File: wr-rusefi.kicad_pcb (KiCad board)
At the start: 2 copper layers, 94 x 94 mm, 147 parts, among them P101 USB_OTG, P102 CONN_01X08, P103 CONN_01X08, P104 CONN_01X04, P105 CONN_01X08, P106 CONN_01X08, P107 CONN_01X02, P108 USB_OTG, P109 CONN_01X02, P110 CONN_01X06, Q401 IRF540N, Q402 IRF540N, Q403 IRF540N, Q404 IRF540N, Q405 IRF540N, Q406 IRF540N, U101 ISL89410, U102 ISL89410, U103 FT230XS, U104 MAX9924, U105 MCP2562-E/SN, U106 LD1117S33TR, U107 MAX9924, U108 ISL89410, U109 STM32F407VGTx, U110 ISL89410, U201 LM324, U301 LM324, U501 LM7805CT, Y101 Crystal

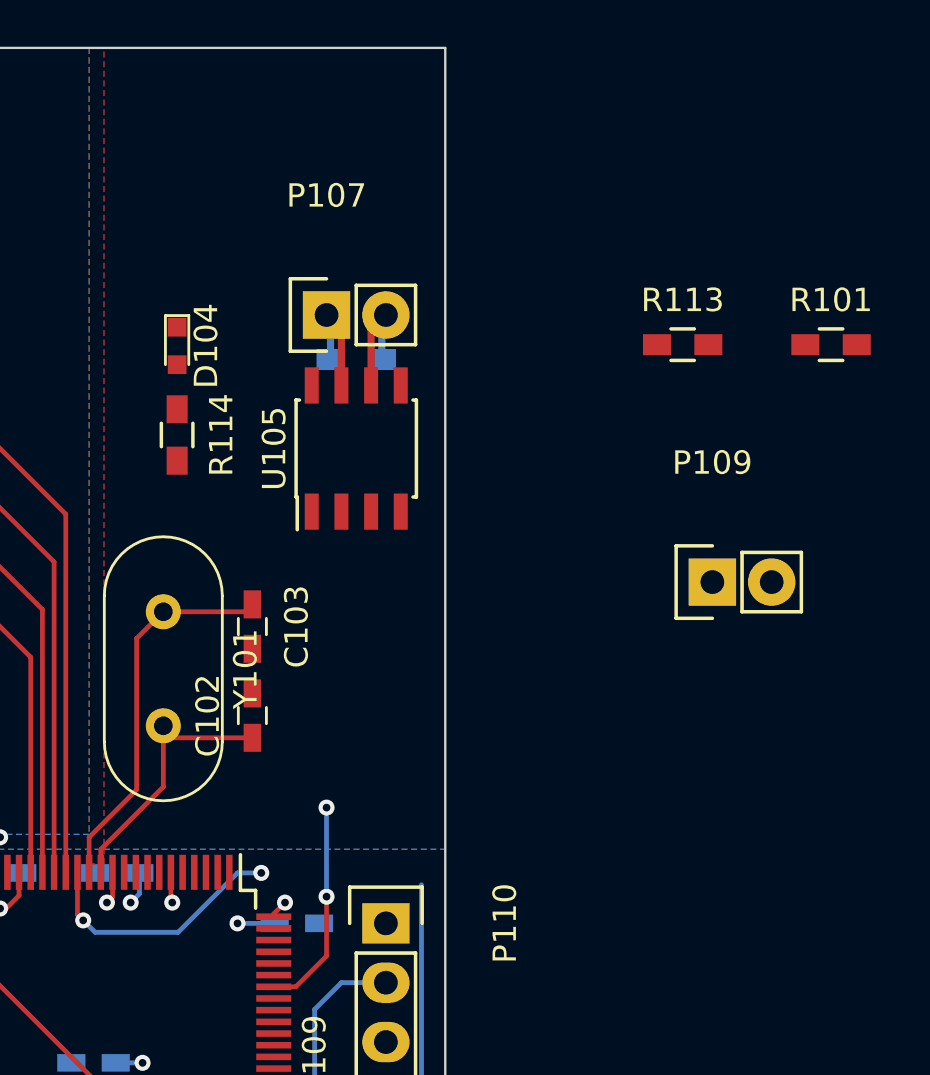
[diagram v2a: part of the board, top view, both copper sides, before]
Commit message: Rough placement of reset & boot0 pullups and jumper
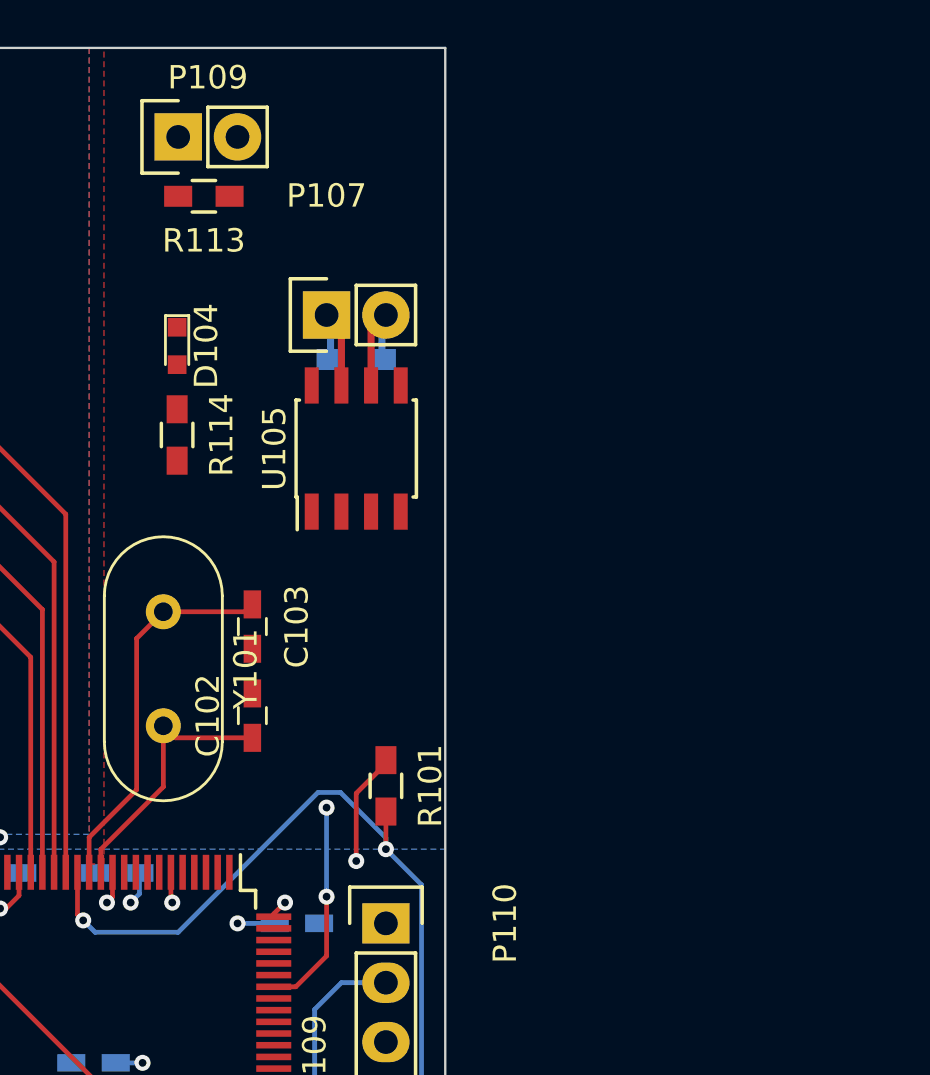
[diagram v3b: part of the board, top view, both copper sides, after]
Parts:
- moved P109 29.8 mm to (133.3, 54.6)
- moved R101 26.8 mm to (142.2, 82.4), turned to 270 degrees
- moved R113 21.5 mm to (134.4, 57.1), turned to 180 degrees
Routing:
- net NRST: track 23.5 -> 35.3 mm
- net +3V3: track 13.7 -> 18.6 mm, vias 8 -> 9
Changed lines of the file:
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@@
     (links 363)
     (no_connects 159)
-    (area 47.1802 29.151866 205.6698 144.830001)
+    (area 47.1802 49.471866 163.619801 144.830001)
     (thickness 1.6)
     (drawings 4)
-    (tracks 929)
+    (tracks 937)
     (zones 0)
     (modules 147)
@@
   )
   (module Socket_Strips:Socket_Strip_Straight_1x02 (layer F.Cu)
-    (at 156.21 73.66)
+    (at 133.35 54.61)
     (descr "Through hole socket strip")
     (tags "socket strip")
-    (fp_text reference P109 (at 0 -5.1) (layer F.SilkS)
+    (fp_text reference P109 (at 1.27 -2.54) (layer F.SilkS)
       (effects (font (size 1 1) (thickness 0.15)))
     )
@@
   )
   (module Resistors_SMD:R_0603_HandSoldering (layer F.Cu)
-    (at 161.29 63.5)
+    (at 142.24 82.38 270)
     (descr "Resistor SMD 0603, hand soldering")
     (tags "resistor 0603")
     (attr smd)
-    (fp_text reference R101 (at 0 -1.9) (layer F.SilkS)
+    (fp_text reference R101 (at 0 -1.9 270) (layer F.SilkS)
       (effects (font (size 1 1) (thickness 0.15)))
     )
-    (fp_text value 10k (at 0 1.9) (layer F.Fab)
+    (fp_text value 10k (at 0 1.9 270) (layer F.Fab)
       (effects (font (size 1 1) (thickness 0.15)))
     )
@@
     (fp_line (start 0.5 0.675) (end -0.5 0.675) (layer F.SilkS) (width 0.15))
     (fp_line (start -0.5 -0.675) (end 0.5 -0.675) (layer F.SilkS) (width 0.15))
-    (pad 1 smd rect (at -1.1 0) (size 1.2 0.9) (layers F.Cu F.Paste F.Mask)
+    (pad 1 smd rect (at -1.1 0 270) (size 1.2 0.9) (layers F.Cu F.Paste F.Mask)
       (net 7 +3V3))
-    (pad 2 smd rect (at 1.1 0) (size 1.2 0.9) (layers F.Cu F.Paste F.Mask)
+    (pad 2 smd rect (at 1.1 0 270) (size 1.2 0.9) (layers F.Cu F.Paste F.Mask)
       (net 94 NRST))
     (model Resistors_SMD.3dshapes/R_0603_HandSoldering.wrl
@@
   )
   (module Resistors_SMD:R_0603_HandSoldering (layer F.Cu)
-    (at 154.94 63.5)
+    (at 134.45 57.15 180)
     (descr "Resistor SMD 0603, hand soldering")
     (tags "resistor 0603")
     (attr smd)
-    (fp_text reference R113 (at 0 -1.9) (layer F.SilkS)
+    (fp_text reference R113 (at 0 -1.9 180) (layer F.SilkS)
       (effects (font (size 1 1) (thickness 0.15)))
     )
-    (fp_text value 10k (at 0 1.9) (layer F.Fab)
+    (fp_text value 10k (at 0 1.9 180) (layer F.Fab)
       (effects (font (size 1 1) (thickness 0.15)))
     )
@@
     (fp_line (start 0.5 0.675) (end -0.5 0.675) (layer F.SilkS) (width 0.15))
     (fp_line (start -0.5 -0.675) (end 0.5 -0.675) (layer F.SilkS) (width 0.15))
-    (pad 1 smd rect (at -1.1 0) (size 1.2 0.9) (layers F.Cu F.Paste F.Mask)
+    (pad 1 smd rect (at -1.1 0 180) (size 1.2 0.9) (layers F.Cu F.Paste F.Mask)
       (net 7 +3V3))
-    (pad 2 smd rect (at 1.1 0) (size 1.2 0.9) (layers F.Cu F.Paste F.Mask)
+    (pad 2 smd rect (at 1.1 0 180) (size 1.2 0.9) (layers F.Cu F.Paste F.Mask)
       (net 91 "Net-(P109-Pad1)"))
     (model Resistors_SMD.3dshapes/R_0603_HandSoldering.wrl
@@
   (segment (start 97.63 58.42) (end 96.52 58.42) (width 0.3048) (layer F.Cu) (net 6))
   (via (at 96.52 58.42) (size 0.6858) (drill 0.3302) (layers F.Cu B.Cu) (net 6))
+  (segment (start 142.24 81.28) (end 142.24 81.43) (width 0.2032) (layer F.Cu) (net 7))
+  (segment (start 142.24 81.43) (end 140.97 82.7) (width 0.2032) (layer F.Cu) (net 7))
+  (segment (start 140.97 82.7) (end 140.97 85.598) (width 0.2032) (layer F.Cu) (net 7))
+  (via (at 140.97 85.598) (size 0.6858) (drill 0.3302) (layers F.Cu B.Cu) (net 7))
   (segment (start 133.04 86.08) (end 133.04 87.32) (width 0.2032) (layer F.Cu) (net 7))
   (segment (start 133.04 87.32) (end 133.096 87.376) (width 0.2032) (layer F.Cu) (net 7))
@@
   (segment (start 136.144 104.394) (end 140.462 100.076) (width 0.2032) (layer B.Cu) (net 93))
   (segment (start 134.874 104.394) (end 136.144 104.394) (width 0.2032) (layer B.Cu) (net 93))
+  (segment (start 129.286 88.138) (end 129.794 88.646) (width 0.2032) (layer B.Cu) (net 94))
+  (segment (start 133.35 88.646) (end 139.331701 82.664299) (width 0.2032) (layer B.Cu) (net 94))
+  (segment (start 129.794 88.646) (end 133.35 88.646) (width 0.2032) (layer B.Cu) (net 94))
+  (segment (start 139.331701 82.664299) (end 140.299232 82.664299) (width 0.2032) (layer B.Cu) (net 94))
+  (segment (start 140.299232 82.664299) (end 142.24 84.605067) (width 0.2032) (layer B.Cu) (net 94))
+  (segment (start 142.24 84.605067) (end 142.24 85.09) (width 0.2032) (layer B.Cu) (net 94))
+  (segment (start 142.24 85.09) (end 142.24 83.48) (width 0.2032) (layer F.Cu) (net 94))
+  (segment (start 143.764 86.614) (end 142.24 85.09) (width 0.2032) (layer B.Cu) (net 94))
+  (via (at 142.24 85.09) (size 0.6858) (drill 0.3302) (layers F.Cu B.Cu) (net 94))
   (segment (start 143.764 96.901) (end 143.764 86.614) (width 0.2032) (layer B.Cu) (net 94))
   (segment (start 142.24 98.425) (end 143.764 96.901) (width 0.2032) (layer B.Cu) (net 94))
-  (segment (start 133.35 88.646) (end 135.89 86.106) (width 0.2032) (layer B.Cu) (net 94))
-  (segment (start 135.89 86.106) (end 136.906 86.106) (width 0.2032) (layer B.Cu) (net 94))
-  (via (at 136.906 86.106) (size 0.6858) (drill 0.3302) (layers F.Cu B.Cu) (net 94))
-  (segment (start 129.794 88.646) (end 133.35 88.646) (width 0.2032) (layer B.Cu) (net 94))
-  (segment (start 129.286 88.138) (end 129.794 88.646) (width 0.2032) (layer B.Cu) (net 94))
   (segment (start 129.04 86.08) (end 129.04 87.892) (width 0.2032) (layer F.Cu) (net 94))
   (segment (start 129.04 87.892) (end 129.286 88.138) (width 0.2032) (layer F.Cu) (net 94))
@@
     (connect_pads (clearance 0.2032))
     (min_thickness 0.2032)
-    (fill (arc_segments 16) (thermal_gap 0.2032) (thermal_bridge_width 0.508))
+    (fill yes (arc_segments 16) (thermal_gap 0.2032) (thermal_bridge_width 0.508))
     (polygon
       (pts
@@
     (connect_pads (clearance 0.2032))
     (min_thickness 0.2032)
-    (fill (arc_segments 16) (thermal_gap 0.2032) (thermal_bridge_width 0.2286))
+    (fill yes (arc_segments 16) (thermal_gap 0.2032) (thermal_bridge_width 0.2286))
     (polygon
       (pts
@@
     (connect_pads (clearance 0.2032))
     (min_thickness 0.2032)
-    (fill (arc_segments 16) (thermal_gap 0.2032) (thermal_bridge_width 0.2286))
+    (fill yes (arc_segments 16) (thermal_gap 0.2032) (thermal_bridge_width 0.2286))
     (polygon
       (pts
@@
     (connect_pads (clearance 0.0254))
     (min_thickness 0.0254)
-    (fill (arc_segments 16) (thermal_gap 0.254) (thermal_bridge_width 0.762))
+    (fill yes (arc_segments 16) (thermal_gap 0.254) (thermal_bridge_width 0.762))
     (polygon
       (pts
@@
     (connect_pads (clearance 0.0254))
     (min_thickness 0.0254)
-    (fill (arc_segments 16) (thermal_gap 0.254) (thermal_bridge_width 0.762))
+    (fill yes (arc_segments 16) (thermal_gap 0.254) (thermal_bridge_width 0.762))
     (polygon
       (pts
@@
     (connect_pads (clearance 0.0254))
     (min_thickness 0.0254)
-    (fill (arc_segments 16) (thermal_gap 0.254) (thermal_bridge_width 0.762))
+    (fill yes (arc_segments 16) (thermal_gap 0.254) (thermal_bridge_width 0.762))
     (polygon
       (pts
@@
     (connect_pads (clearance 0.2032))
     (min_thickness 0.2032)
-    (fill (arc_segments 16) (thermal_gap 0.2032) (thermal_bridge_width 0.508))
+    (fill yes (arc_segments 16) (thermal_gap 0.2032) (thermal_bridge_width 0.508))
     (polygon
       (pts
@@
     (connect_pads (clearance 0.2032))
     (min_thickness 0.2032)
-    (fill (arc_segments 16) (thermal_gap 0.2032) (thermal_bridge_width 0.508))
+    (fill yes (arc_segments 16) (thermal_gap 0.2032) (thermal_bridge_width 0.508))
     (polygon
       (pts

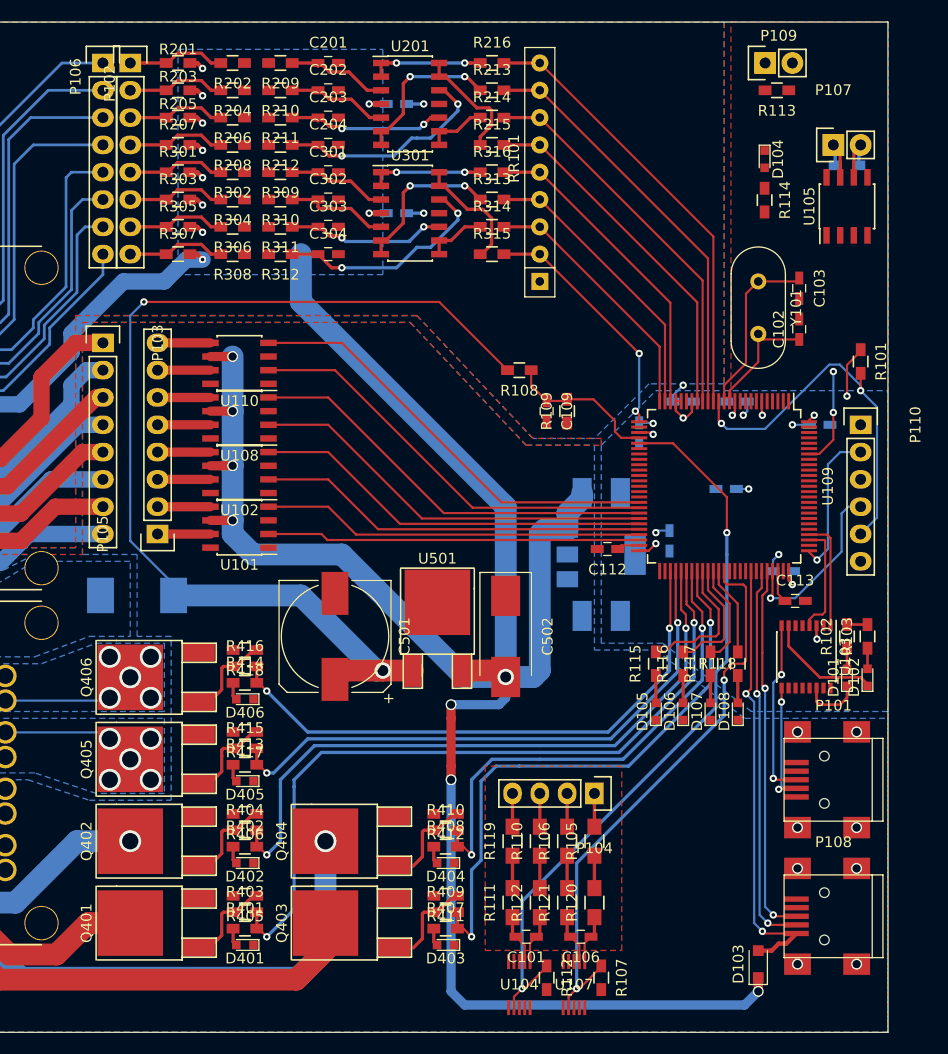
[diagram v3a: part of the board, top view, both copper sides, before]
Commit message: Move CAN to PD0/1, nearly done routing
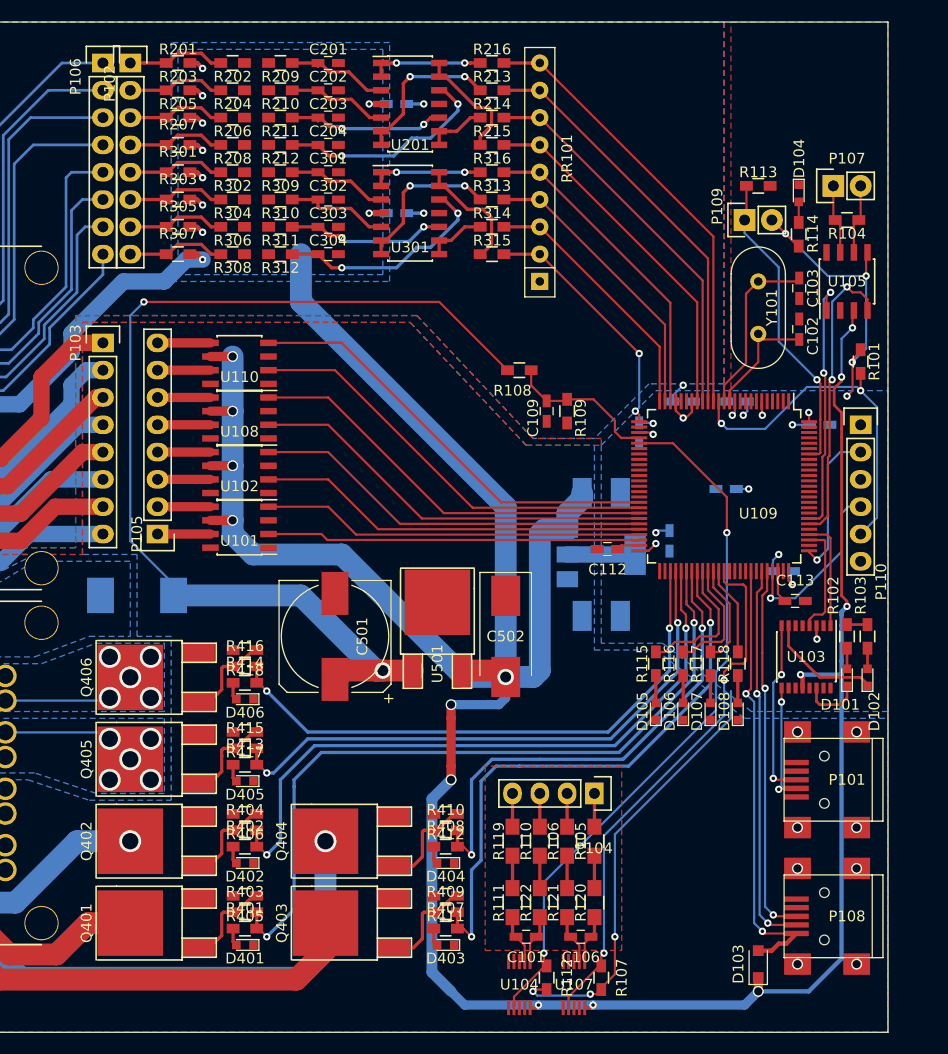
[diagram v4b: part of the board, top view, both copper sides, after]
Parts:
- R104: moved to F.Cu
- moved P109 14.7 mm to (131.4, 69.2)
- moved R113 9.06 mm to (132.7, 66.0), turned to 0 degrees
- moved U105 6.99 mm to (141.0, 74.9)
- moved R104 5.08 mm to (141.0, 69.2)
- moved D104 4.49 mm to (136.5, 66.7)
- moved R114 4.49 mm to (136.5, 70.5)
- moved P107 3.81 mm to (139.7, 66.0)
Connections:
- C112 pad 2: GND -> Net-(C112-Pad2)
- R113 pad 1: +3V3 -> Net-(P109-Pad1)
- R113 pad 2: Net-(P109-Pad1) -> GND
- U109 pad 51: CAN_RX -> Net-(U109-Pad51)
- U109 pad 81: Net-(U109-Pad81) -> CAN_RX
- U109 pad 82: Net-(U109-Pad82) -> CAN_TX
- U109 pad 92: CAN_TX -> Net-(U109-Pad92)
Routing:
- net +5V: track 240.0 -> 319.1 mm, vias 18 -> 24
- net +3V3: track 18.6 -> 89.3 mm, vias 9 -> 15
- net CAN_RX: track 0.00 -> 27.5 mm, vias 0 -> 2
- net CAN_TX: track 0.00 -> 24.4 mm, vias 0 -> 2
- net Net-(P109-Pad1): track 9.16 -> 28.9 mm, vias 2 -> 1
- net VRIN1: track 53.0 -> 49.9 mm
- net VRIN2: track 69.1 -> 66.2 mm
- net NRST: track 35.3 -> 33.3 mm
- net Net-(D104-Pad2): track 0.00 -> 1.91 mm
- net CANL: track 5.25 -> 6.45 mm
- net CANH: track 5.25 -> 6.45 mm
